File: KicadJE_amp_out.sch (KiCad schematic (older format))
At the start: 33 parts, among them J301 Tone/Noise, J302 RND, J303 Noise, J304 DRUM_OUT, J305 Tones, J306 Noise, U101 74HC04, U302 TL072

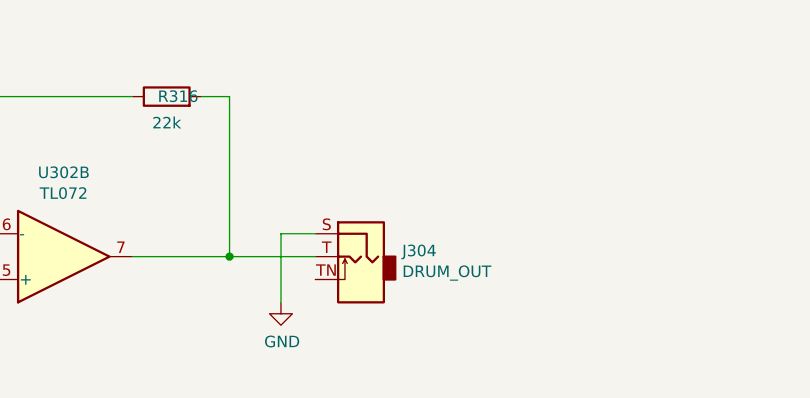
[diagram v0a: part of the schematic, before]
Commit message: Breadboard routed
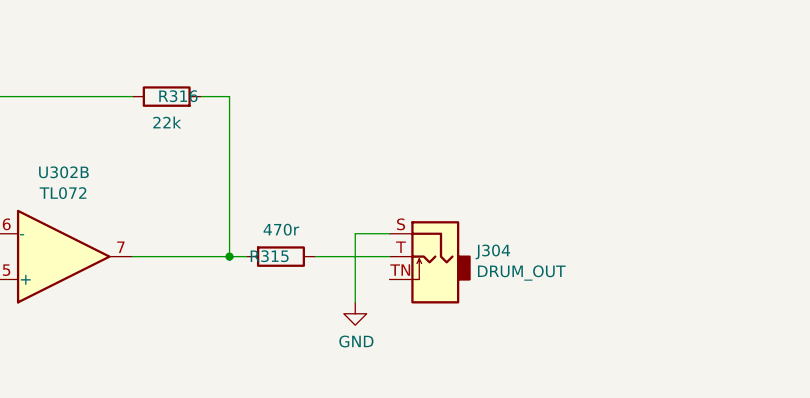
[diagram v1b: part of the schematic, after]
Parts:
- added R315: 470r, AJ:R_0805_AJ, symbol Device:R
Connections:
- net at R316.2, U302.7: now also R315.2; no longer J304.T
- new net: J304.T, R315.1
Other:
- moved on the sheet: J304
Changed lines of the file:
@@
 L Connector:AudioJack2_SwitchT J?
 U 1 1 61BE2ABB
-P 6000 4900
+P 6325 4900
 AR Path="/607E07E1/61BE2ABB" Ref="J?"  Part="1"
 AR Path="/61BE2ABB" Ref="J?"  Part="1"
 AR Path="/6165D4D0/61BE2ABB" Ref="J304"  Part="1"
-F 0 "J304" H 5820 4925 50  0000 R CNN
-F 1 "DRUM_OUT" H 5820 4834 50  0000 R CNN
-F 2 "Connector_Audio:Jack_3.5mm_QingPu_WQP-PJ398SM_Vertical_CircularHoles" H 6000 4900 50  0001 C CNN
-F 3 "~" H 6000 4900 50  0001 C CNN
-	1    6000 4900
+F 0 "J304" H 6145 4925 50  0000 R CNN
+F 1 "DRUM_OUT" H 6145 4834 50  0000 R CNN
+F 2 "Connector_Audio:Jack_3.5mm_QingPu_WQP-PJ398SM_Vertical_CircularHoles" H 6325 4900 50  0001 C CNN
+F 3 "~" H 6325 4900 50  0001 C CNN
+	1    6325 4900
 	-1   0    0    -1
 $EndComp
-Wire Wire Line
-	5425 4900 5800 4900
-Connection ~ 5425 4900
 $Comp
 L power:GND #PWR?
 U 1 1 61BE53DA
-P 5650 5100
+P 5975 5100
 AR Path="/61BE53DA" Ref="#PWR?"  Part="1"
 AR Path="/607E07E1/61BE53DA" Ref="#PWR?"  Part="1"
 AR Path="/6165D4D0/61BE53DA" Ref="#PWR0306"  Part="1"
-F 0 "#PWR0306" H 5650 4850 50  0001 C CNN
-F 1 "GND" H 5655 4927 50  0000 C CNN
-F 2 "" H 5650 5100 50  0001 C CNN
-F 3 "" H 5650 5100 50  0001 C CNN
-	1    5650 5100
+F 0 "#PWR0306" H 5975 4850 50  0001 C CNN
+F 1 "GND" H 5980 4927 50  0000 C CNN
+F 2 "" H 5975 5100 50  0001 C CNN
+F 3 "" H 5975 5100 50  0001 C CNN
+	1    5975 5100
 	1    0    0    -1
 $EndComp
 Wire Wire Line
-	5800 4800 5650 4800
+	6125 4800 5975 4800
 Wire Wire Line
-	5650 4800 5650 5100
+	5975 4800 5975 5100
 Text GLabel 9800 1775 0    47   Input ~ 0
 NoiseOut
@@
 Wire Wire Line
 	2200 1000 3050 1000
+Wire Wire Line
+	5425 4900 5500 4900
+Connection ~ 5425 4900
+$Comp
+L Device:R R?
+U 1 1 609EDEE3
+P 5650 4900
+AR Path="/609EDEE3" Ref="R?"  Part="1"
+AR Path="/5C8C5FC0/609EDEE3" Ref="R?"  Part="1"
+AR Path="/5D60ED9A/609EDEE3" Ref="R?"  Part="1"
+AR Path="/60565919/609EDEE3" Ref="R?"  Part="1"
+AR Path="/6165D4D0/609EDEE3" Ref="R315"  Part="1"
+F 0 "R315" V 5650 4850 50  0000 C CNN
+F 1 "470r" V 5534 4900 50  0000 C CNN
+F 2 "AJ:R_0805_AJ" V 5580 4900 50  0001 C CNN
+F 3 "~" H 5650 4900 50  0001 C CNN
+	1    5650 4900
+	0    1    1    0
+$EndComp
+Wire Wire Line
+	5800 4900 6125 4900
 $EndSCHEMATC

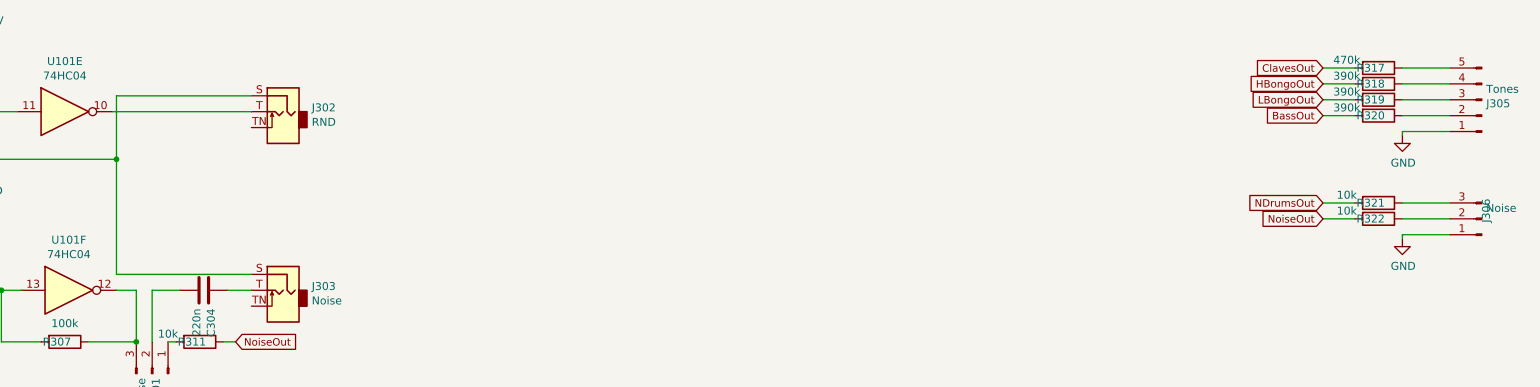
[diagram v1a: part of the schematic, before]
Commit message: BB Logo - GND planes
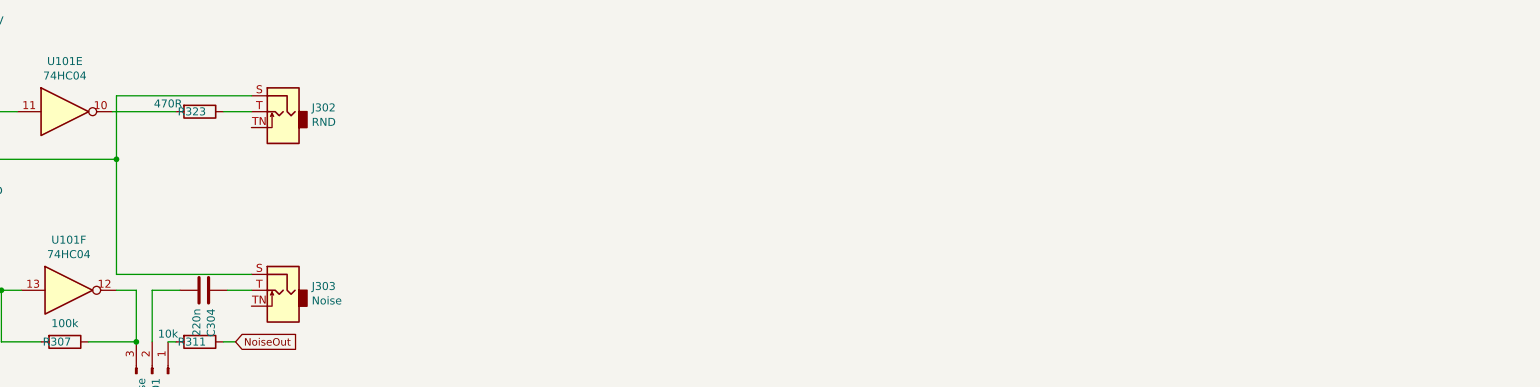
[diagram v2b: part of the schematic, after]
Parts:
- removed J305: Tones, Connector_PinHeader_2.54mm:PinHeader_1x05_P2.54mm_Vertical, symbol Connector:Conn_01x05_Male
- removed J306: Noise, Connector_PinHeader_2.54mm:PinHeader_1x03_P2.54mm_Vertical, symbol Connector:Conn_01x03_Male
- removed R317: 470k, AJ:R_0805_AJ, symbol Device:R
- removed R318, R319, R320: 390k, AJ:R_0805_AJ, symbol Device:R
- removed R321, R322: 10k, AJ:R_0805_AJ, symbol Device:R
- added R323: 470R, AJ:R_0805_AJ, symbol Device:R
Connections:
- net at J302.T: now also R323.1; no longer U101.10
- new net: R323.2, U101.10
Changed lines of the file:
@@
 	2200 1400 1400 1400
 Connection ~ 1400 1400
-$Comp
-L Connector:Conn_01x05_Male J?
-U 1 1 616A3B0C
-P 10800 1025
-AR Path="/607E07E1/616A3B0C" Ref="J?"  Part="1"
-AR Path="/616A3B0C" Ref="J?"  Part="1"
-AR Path="/6165D4D0/616A3B0C" Ref="J305"  Part="1"
-F 0 "J305" H 10772 1049 50  0000 R CNN
-F 1 "Tones" H 10772 958 50  0000 R CNN
-F 2 "Connector_PinHeader_2.54mm:PinHeader_1x05_P2.54mm_Vertical" H 10800 1025 50  0001 C CNN
-F 3 "~" H 10800 1025 50  0001 C CNN
-	1    10800 1025
-	-1   0    0    1
-$EndComp
-Text GLabel 9800 1025 0    47   Input ~ 0
-LBongoOut
-Text GLabel 9800 1125 0    47   Input ~ 0
-BassOut
-Text GLabel 9800 825  0    47   Input ~ 0
-ClavesOut
-Text GLabel 9800 925  0    47   Input ~ 0
-HBongoOut
-Wire Wire Line
-	10600 1125 10300 1125
-Wire Wire Line
-	10300 1025 10600 1025
-Wire Wire Line
-	10600 925  10300 925
-Wire Wire Line
-	10600 825  10300 825
-$Comp
-L power:GND #PWR?
-U 1 1 616A3B1A
-P 10300 1250
-AR Path="/616A3B1A" Ref="#PWR?"  Part="1"
-AR Path="/6165D4D0/616A3B1A" Ref="#PWR0307"  Part="1"
-F 0 "#PWR0307" H 10300 1000 50  0001 C CNN
-F 1 "GND" H 10305 1077 50  0000 C CNN
-F 2 "" H 10300 1250 50  0001 C CNN
-F 3 "" H 10300 1250 50  0001 C CNN
-	1    10300 1250
-	1    0    0    -1
-$EndComp
-Wire Wire Line
-	10300 1250 10300 1225
-Wire Wire Line
-	10300 1225 10600 1225
 Text GLabel 1275 5375 0    47   Input ~ 0
 NDrumsOut
@@
 Wire Wire Line
 	2325 2225 2200 2225
-$Comp
-L Connector:Conn_01x03_Male J?
-U 1 1 61710EAB
-P 10800 1775
-AR Path="/607E07E1/61710EAB" Ref="J?"  Part="1"
-AR Path="/61710EAB" Ref="J?"  Part="1"
-AR Path="/6165D4D0/61710EAB" Ref="J306"  Part="1"
-F 0 "J306" V 10772 1799 50  0000 R CNN
-F 1 "Noise" H 10772 1708 50  0000 R CNN
-F 2 "Connector_PinHeader_2.54mm:PinHeader_1x03_P2.54mm_Vertical" H 10800 1775 50  0001 C CNN
-F 3 "~" H 10800 1775 50  0001 C CNN
-	1    10800 1775
-	-1   0    0    1
-$EndComp
-$Comp
-L power:GND #PWR?
-U 1 1 61715219
-P 10300 1900
-AR Path="/61715219" Ref="#PWR?"  Part="1"
-AR Path="/6165D4D0/61715219" Ref="#PWR0308"  Part="1"
-F 0 "#PWR0308" H 10300 1650 50  0001 C CNN
-F 1 "GND" H 10305 1727 50  0000 C CNN
-F 2 "" H 10300 1900 50  0001 C CNN
-F 3 "" H 10300 1900 50  0001 C CNN
-	1    10300 1900
-	1    0    0    -1
-$EndComp
-Wire Wire Line
-	10300 1900 10300 1875
-Text GLabel 9800 1675 0    47   Input ~ 0
-NDrumsOut
-Wire Wire Line
-	10300 1875 10600 1875
-Wire Wire Line
-	10600 1775 10300 1775
-Wire Wire Line
-	10600 1675 10300 1675
 $Comp
 L Connector:AudioJack2_SwitchT J?
@@
 Wire Wire Line
 	5975 4800 5975 5100
-Text GLabel 9800 1775 0    47   Input ~ 0
-NoiseOut
 Text GLabel 2950 2550 2    47   Input ~ 0
 NoiseOut
-$Comp
-L Device:R R?
-U 1 1 608AC9E1
-P 10150 925
-AR Path="/608AC9E1" Ref="R?"  Part="1"
-AR Path="/5C8C5FC0/608AC9E1" Ref="R?"  Part="1"
-AR Path="/5D60ED9A/608AC9E1" Ref="R?"  Part="1"
-AR Path="/60565919/608AC9E1" Ref="R?"  Part="1"
-AR Path="/6165D4D0/608AC9E1" Ref="R318"  Part="1"
-F 0 "R318" V 10150 875 50  0000 C CNN
-F 1 "390k" V 10100 725 50  0000 C CNN
-F 2 "AJ:R_0805_AJ" V 10080 925 50  0001 C CNN
-F 3 "~" H 10150 925 50  0001 C CNN
-	1    10150 925
-	0    1    1    0
-$EndComp
-$Comp
-L Device:R R?
-U 1 1 608ACE07
-P 10150 825
-AR Path="/608ACE07" Ref="R?"  Part="1"
-AR Path="/5C8C5FC0/608ACE07" Ref="R?"  Part="1"
-AR Path="/5D60ED9A/608ACE07" Ref="R?"  Part="1"
-AR Path="/60565919/608ACE07" Ref="R?"  Part="1"
-AR Path="/6165D4D0/608ACE07" Ref="R317"  Part="1"
-F 0 "R317" V 10150 775 50  0000 C CNN
-F 1 "470k" V 10100 625 50  0000 C CNN
-F 2 "AJ:R_0805_AJ" V 10080 825 50  0001 C CNN
-F 3 "~" H 10150 825 50  0001 C CNN
-	1    10150 825
-	0    1    1    0
-$EndComp
-$Comp
-L Device:R R?
-U 1 1 608ACE11
-P 10150 1025
-AR Path="/608ACE11" Ref="R?"  Part="1"
-AR Path="/5C8C5FC0/608ACE11" Ref="R?"  Part="1"
-AR Path="/5D60ED9A/608ACE11" Ref="R?"  Part="1"
-AR Path="/60565919/608ACE11" Ref="R?"  Part="1"
-AR Path="/6165D4D0/608ACE11" Ref="R319"  Part="1"
-F 0 "R319" V 10150 975 50  0000 C CNN
-F 1 "390k" V 10100 825 50  0000 C CNN
-F 2 "AJ:R_0805_AJ" V 10080 1025 50  0001 C CNN
-F 3 "~" H 10150 1025 50  0001 C CNN
-	1    10150 1025
-	0    1    1    0
-$EndComp
-$Comp
-L Device:R R?
-U 1 1 608ACE1B
-P 10150 1125
-AR Path="/608ACE1B" Ref="R?"  Part="1"
-AR Path="/5C8C5FC0/608ACE1B" Ref="R?"  Part="1"
-AR Path="/5D60ED9A/608ACE1B" Ref="R?"  Part="1"
-AR Path="/60565919/608ACE1B" Ref="R?"  Part="1"
-AR Path="/6165D4D0/608ACE1B" Ref="R320"  Part="1"
-F 0 "R320" V 10150 1075 50  0000 C CNN
-F 1 "390k" V 10100 925 50  0000 C CNN
-F 2 "AJ:R_0805_AJ" V 10080 1125 50  0001 C CNN
-F 3 "~" H 10150 1125 50  0001 C CNN
-	1    10150 1125
-	0    1    1    0
-$EndComp
-Wire Wire Line
-	9800 825  10000 825
-Wire Wire Line
-	10000 1125 9800 1125
-Wire Wire Line
-	9800 1025 10000 1025
-Wire Wire Line
-	10000 925  9800 925
-$Comp
-L Device:R R?
-U 1 1 608B8687
-P 10150 1675
-AR Path="/608B8687" Ref="R?"  Part="1"
-AR Path="/5C8C5FC0/608B8687" Ref="R?"  Part="1"
-AR Path="/5D60ED9A/608B8687" Ref="R?"  Part="1"
-AR Path="/60565919/608B8687" Ref="R?"  Part="1"
-AR Path="/6165D4D0/608B8687" Ref="R321"  Part="1"
-F 0 "R321" V 10150 1625 50  0000 C CNN
-F 1 "10k" V 10100 1475 50  0000 C CNN
-F 2 "AJ:R_0805_AJ" V 10080 1675 50  0001 C CNN
-F 3 "~" H 10150 1675 50  0001 C CNN
-	1    10150 1675
-	0    1    1    0
-$EndComp
-$Comp
-L Device:R R?
-U 1 1 608B8FB9
-P 10150 1775
-AR Path="/608B8FB9" Ref="R?"  Part="1"
-AR Path="/5C8C5FC0/608B8FB9" Ref="R?"  Part="1"
-AR Path="/5D60ED9A/608B8FB9" Ref="R?"  Part="1"
-AR Path="/60565919/608B8FB9" Ref="R?"  Part="1"
-AR Path="/6165D4D0/608B8FB9" Ref="R322"  Part="1"
-F 0 "R322" V 10150 1725 50  0000 C CNN
-F 1 "10k" V 10100 1575 50  0000 C CNN
-F 2 "AJ:R_0805_AJ" V 10080 1775 50  0001 C CNN
-F 3 "~" H 10150 1775 50  0001 C CNN
-	1    10150 1775
-	0    1    1    0
-$EndComp
-Wire Wire Line
-	10000 1775 9800 1775
-Wire Wire Line
-	9800 1675 10000 1675
 Wire Wire Line
 	4325 4200 5000 4200
@@
 	2200 2125 3050 2125
 Wire Wire Line
-	2175 1100 3050 1100
+	2175 1100 2575 1100
 Wire Wire Line
 	2200 1000 3050 1000
@@
 Wire Wire Line
 	5800 4900 6125 4900
+$Comp
+L Device:R R?
+U 1 1 60B239DF
+P 2725 1100
+AR Path="/60B239DF" Ref="R?"  Part="1"
+AR Path="/5C8C5FC0/60B239DF" Ref="R?"  Part="1"
+AR Path="/5D60ED9A/60B239DF" Ref="R?"  Part="1"
+AR Path="/60565919/60B239DF" Ref="R?"  Part="1"
+AR Path="/6165D4D0/60B239DF" Ref="R323"  Part="1"
+F 0 "R323" V 2725 1050 50  0000 C CNN
+F 1 "470R" V 2675 900 50  0000 C CNN
+F 2 "AJ:R_0805_AJ" V 2655 1100 50  0001 C CNN
+F 3 "~" H 2725 1100 50  0001 C CNN
+	1    2725 1100
+	0    1    1    0
+$EndComp
+Wire Wire Line
+	2875 1100 3050 1100
 $EndSCHEMATC
